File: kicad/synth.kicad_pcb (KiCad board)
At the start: 2 copper layers, 190.5 x 101.6 mm, 265 parts, among them CON101 SD_Card, CON201 K375A (DJK-02A), J301 KATE_3.5MM_6, J302 KATE_3.5MM_6, J401 KATE_3.5MM_6, J402 KATE_3.5MM_6, J403 KATE_3.5MM_6, P101 CONN_01X05, P102 CONN_01X03, P103 CONN_01X03, P104 47346-0001, P105 CONN_01X01, P106 DIN_5, P301 CONN_02X04, Q101 MMBTA42, Q201 FDS6675, Q202 IRF7313PBF, Q301 Si2301DS, SW101 SW_PUSH, SW102 SW_PUSH, T201 TRANS_CUSTOM, U101 STM32F405R, U102 USBLC6-2, U103 AD1955, U104 HCPL0453, U201 LM78L12ACZ, U202 79L12, U203 MC33269-SO8, U204 TPS76333DBV, U205 LP2985LV, U206 LP2985LV, U301 OP275S, U302 OP275S, U303 LM4864, U304 LM4864, U305 OP275S, U401 AD824, Y101 25MHz

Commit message: before moving headphone amp to the left
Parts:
- added P302: CONN_01X03, Pin_Headers:Pin_Header_Straight_1x03, F.Cu at (8.64, 135.5)
- added Q401: Si2301DS, TO_SOT_Packages_SMD:SOT-23, F.Cu at (110.7, 142.5)
- added Q402: Si2301DS, TO_SOT_Packages_SMD:SOT-23, F.Cu at (80.3, 142.0)
- added Q403: Si2301DS, TO_SOT_Packages_SMD:SOT-23, F.Cu at (95.2, 142.2)
- added R421: 10K, Resistors_SMD:R_0805, F.Cu at (110.7, 139.2)
- added R422: 10K, Resistors_SMD:R_0805, F.Cu at (80.0, 135.9)
- added R423: 10K, Resistors_SMD:R_0805, F.Cu at (93.7, 135.9)
- R301, R302, R307, R308: footprint Resistors_SMD:R_0805 -> Resistors_SMD:R_1206
- moved R337 149.0 mm to (12.1, 134.6), turned to 90 degrees
- moved J302 149.0 mm to (5.97, 139.7)
- moved C416 148.3 mm to (155.2, 183.6)
- moved C341 141.8 mm to (9.53, 130.2), turned to 270 degrees
- moved J301 140.6 mm to (42.3, 139.7)
- moved C417 139.6 mm to (129.5, 183.6)
- moved R335 138.8 mm to (12.1, 129.5), turned to 270 degrees
- moved L303 137.3 mm to (49.5, 139.3), turned to 180 degrees
- moved R333 136.5 mm to (12.1, 125.7), turned to 90 degrees
- moved R338 136.0 mm to (0.00, 134.6), turned to 90 degrees
- moved C340 135.6 mm to (6.08, 129.9), turned to 0 degrees
- moved C335 134.3 mm to (14.6, 125.7)
- moved C331 133.7 mm to (48.9, 134.9), turned to 0 degrees
- moved R324 133.1 mm to (14.6, 121.9), turned to 270 degrees
- moved U303 131.9 mm to (48.9, 128.0), turned to 180 degrees
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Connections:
- C318 pad 2: Net-(C318-Pad2) -> GNDA
- C320 pad 2: Net-(C318-Pad2) -> GNDA
- C321 pad 2: Net-(C321-Pad2) -> GNDA
- C322 pad 2: Net-(C322-Pad2) -> GNDA
- C323 pad 2: Net-(C321-Pad2) -> GNDA
- C324 pad 2: Net-(C322-Pad2) -> GNDA
- C336 pad 2: Net-(C336-Pad2) -> GNDA
- C338 pad 2: Net-(C336-Pad2) -> GNDA
- C339 pad 2: Net-(C339-Pad2) -> GNDA
- C340 pad 2: Net-(C339-Pad2) -> GNDA
- J301 pad 1: /audioout/~SHUTDOWN -> /audioout/PHONES_SW
- J301 pad 4: /audioout/~SHUTDOWN -> /audioout/PHONES_SW
- Q301 pad 1: /audioout/~SHUTDOWN -> /audioout/PHONES_SW
- R340 pad 2: /audioout/~SHUTDOWN -> /audioout/PHONES_SW
- R401 pad 2: /audio/LEDPLUG1 -> Net-(Q402-Pad2)
- R402 pad 2: /audio/LEDPLUG2 -> Net-(Q403-Pad2)
- R403 pad 2: /audio/LEDPLUG3 -> Net-(Q401-Pad2)
- U101 pad 40: /audio/LEDPLUG2 -> /LEDPLUG2
- U101 pad 41: /audio/LEDPLUG3 -> /LEDPLUG3
- U101 pad 52: /audio/LEDPLUG1 -> /LEDPLUG1
- U101 pad 62: Net-(U101-Pad62) -> /audioout/PHONES_SW
- U303 pad 1: /audioout/~SHUTDOWN -> /audioout/PHONES_SW
- U304 pad 1: /audioout/~SHUTDOWN -> /audioout/PHONES_SW
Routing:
- net GNDA: track 0.00 -> 366.9 mm, vias 0 -> 22
- net +12VOPA: track 0.00 -> 119.6 mm, vias 0 -> 5
- net -12VOPA: track 0.00 -> 116.2 mm, vias 0 -> 4
- net +3V3A_CPU: track 0.00 -> 112.4 mm
- net /audioout/SE_RIGHT: track 0.00 -> 108.6 mm, vias 0 -> 2
- net /audioout/IOUTR+: track 0.00 -> 97.0 mm
- net /audioout/IOUTR-: track 0.00 -> 80.2 mm
- net /audioout/SE_LEFT: track 0.00 -> 80.2 mm, vias 0 -> 2
- net /audioout/VREF: track 0.00 -> 65.1 mm, vias 0 -> 3
- net GNDD: track 0.00 -> 57.9 mm, vias 0 -> 1
- net /audioout/IOUTL+: track 0.00 -> 56.3 mm
- net (no net): track 0.00 -> 55.5 mm, vias 0 -> 1
- net /audioout/IOUTL-: track 0.00 -> 54.5 mm
- net Net-(C328-Pad1): track 0.00 -> 46.5 mm
- net /audioout/PHONES_SW: track 0.00 -> 42.6 mm
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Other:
- net class Default: via_dia 0.6 -> 1.25
- net class anal added: clearance 0.2, trace_width 0.25, via_dia 1.25, via_drill 0.4
- net class power added: clearance 0.3, trace_width 0.4, via_dia 1.25, via_drill 0.4

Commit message: gruuuu
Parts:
- added Q302: BC817, TO_SOT_Packages_SMD:SOT-23, F.Cu at (92.6, 90.9)
- added R303: 1K, Resistors_SMD:R_0805, F.Cu at (16.3, 144.5)
- added R342: 10K, Resistors_SMD:R_0805, F.Cu at (96.2, 90.7)
- P105: footprint SMD_Packages:1Pin -> Pin_Headers:Pin_Header_Straight_1x01
- R118: footprint Resistors_SMD:R_0402 -> Resistors_SMD:R_0603
- R203: footprint Resistors_SMD:R_0805 -> Resistors_SMD:R_2010
- T201: footprint Transformers_SMPS_ThroughHole:Coilcraft-Q4434-B_Rhombus-T1311 -> trafo_ossi:TRAFO_OSSI
- moved R120 136.2 mm to (32.6, 73.5)
- moved U104 134.6 mm to (27.2, 74.4)
- moved D102 131.9 mm to (20.7, 76.5), turned to 90 degrees
- moved R116 130.7 mm to (21.3, 72.9), turned to 270 degrees
- moved P106 130.4 mm to (29.0, 60.7)
- moved D103 128.2 mm to (42.8, 53.3), turned to 0 degrees
- moved Q101 124.0 mm to (43.9, 57.7)
- moved R121 119.8 mm to (40.8, 57.8), turned to 90 degrees
- moved R122 119.4 mm to (48.4, 55.0), turned to 135 degrees
- moved BT101 101.9 mm to (80.8, -31.8)
- moved P103 95.1 mm to (81.4, 81.7)
- moved CON101 90.3 mm to (136.2, -8.59)
- moved C114 90.0 mm to (127.6, -12.7)
- moved C115 90.0 mm to (127.6, -16.5)
- moved R112 90.0 mm to (110.5, -10.8)
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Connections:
- net /LEDPLUG1 renamed Net-(U101-Pad52)
- net /LEDPLUG2 renamed Net-(U101-Pad40)
- net /LEDPLUG3 renamed Net-(U101-Pad41)
- C201 pad 1: /megapower/+5V_UNREG -> +5VJACK
- C304 pad 1: /audioout/IOUTL- -> /audioout/IOUTL+
- C304 pad 2: /audioout/IOUTL+ -> /audioout/IOUTL-
- D204 pad 2: /megapower/+15V -> +3V3D_CPU
- J301 pad 1: /audioout/PHONES_SW -> /audioout/~SHUTDOWN
- J301 pad 4: /audioout/PHONES_SW -> /audioout/~SHUTDOWN
- Q201 pad 5: /megapower/+5V_UNREG -> +5VJACK
- Q201 pad 6: /megapower/+5V_UNREG -> +5VJACK
- Q201 pad 7: /megapower/+5V_UNREG -> +5VJACK
- Q201 pad 8: /megapower/+5V_UNREG -> +5VJACK
- Q301 pad 1: /audioout/PHONES_SW -> /audioout/~SHUTDOWN
- R305 pad 2: /audioout/IOUTL+ -> /audioout/IOUTL-
- R309 pad 2: /audioout/IOUTL- -> /audioout/IOUTL+
- R311 pad 1: /audioout/IOUTL- -> /audioout/IOUTL+
- R312 pad 1: /audioout/IOUTL+ -> /audioout/IOUTL-
- R315 pad 1: /audioout/IOUTL+ -> /audioout/IOUTL-
- R318 pad 1: /audioout/IOUTL- -> /audioout/IOUTL+
- R319 pad 2: Net-(C325-Pad1) -> Net-(C326-Pad2)
- R320 pad 2: Net-(C326-Pad2) -> Net-(C325-Pad1)
- R340 pad 2: /audioout/PHONES_SW -> /audioout/~SHUTDOWN
- T201 pad 3: Net-(Q202-Pad5) -> Net-(T201-Pad3)
- T201 pad 4: Net-(D202-Pad1) -> Net-(Q202-Pad5)
- T201 pad 5: GNDPWR -> Net-(D202-Pad1)
- T201 pad 6: Net-(D203-Pad2) -> GNDPWR
- T201 pad 7: Net-(D201-Pad2) -> Net-(D203-Pad2)
- T201 pad 8: (no net) -> Net-(D201-Pad2)
- U301 pad 2: /audioout/IOUTL- -> /audioout/IOUTL+
- U301 pad 6: /audioout/IOUTL+ -> /audioout/IOUTL-
- U303 pad 1: /audioout/PHONES_SW -> /audioout/~SHUTDOWN
- U304 pad 1: /audioout/PHONES_SW -> /audioout/~SHUTDOWN
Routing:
- net +3V3D_CPU: track 0.00 -> 277.7 mm, vias 0 -> 4
- net /megapower/+15V: track 0.00 -> 179.9 mm, vias 0 -> 1
- net GNDA: track 366.9 -> 530.8 mm, vias 22 -> 34
- net /megapower/+7V5: track 0.00 -> 155.7 mm, vias 0 -> 3
- net /megapower/-15V: track 0.00 -> 147.2 mm, vias 0 -> 1
- net +3V3A_CPU: track 112.4 -> 246.9 mm, vias 0 -> 2
- net /MIDI_RX: track 0.00 -> 122.8 mm
- net Net-(Q302-Pad1): track 0.00 -> 122.3 mm, vias 0 -> 2
- net GNDD: track 57.9 -> 149.6 mm, vias 1 -> 15
- net /audio/HIGAIN2: track 10.8 -> 97.8 mm, vias 0 -> 2
- net /audio/POT1: track 0.00 -> 84.9 mm, vias 0 -> 2
- net /audio/PLUG_3: track 19.0 -> 103.4 mm, vias 1 -> 4
- net /audioout/LINEOUT_SW: track 4.21 -> 86.8 mm, vias 0 -> 1
- net /audio/POT2: track 0.00 -> 73.3 mm, vias 0 -> 3
- net /audio/PLUG_2: track 19.5 -> 91.5 mm, vias 1 -> 3
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- added copper zone on B.Cu, net GNDA
- added copper zone on F.Cu, net GNDA
- added copper zone on B.Cu, net GNDD
- added copper zone on F.Cu, net GNDD
- added copper zone on B.Cu, net GNDPWR
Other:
- board size 190.5 x 101.6 mm -> 154.9 x 101.6 mm
- net class power: clearance 0.3 -> 0.2

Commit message: drc ok large vias
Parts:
- C114, C115, R112, R113, R114: moved to F.Cu
- C207, C208: moved to B.Cu
- moved C114 137.2 mm to (31.0, 84.7)
- moved CON101 136.9 mm to (40.1, 89.0), turned to 90 degrees
- moved C115 136.6 mm to (31.6, 80.6)
- moved R114 122.8 mm to (34.5, 89.5), turned to 180 degrees
- moved R112 121.9 mm to (34.5, 84.6), turned to 180 degrees
- moved R113 119.4 mm to (34.5, 87.1), turned to 180 degrees
- moved BT101 102.4 mm to (85.7, 70.5), turned to 90 degrees
- moved C112 42.5 mm to (99.7, 67.7), turned to 90 degrees
- moved D204 35.8 mm to (129.8, 101.7), turned to 135 degrees
- moved R205 3.21 mm to (160.8, 109.7), turned to 180 degrees
- moved C207 2.56 mm to (157.5, 86.4), turned to 180 degrees
- moved C208 1.25 mm to (150.9, 86.4), turned to 180 degrees
- moved R204 1.21 mm to (164.0, 109.7)
- moved R102 0.76 mm to (90.9, 75.5)
- moved C105 0.57 mm to (118.1, 82.9)
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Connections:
- C207 pad 1: GNDPWR -> Net-(C207-Pad1)
- C207 pad 2: GNDPWR -> Net-(C207-Pad2)
- C208 pad 1: GNDPWR -> Net-(C208-Pad1)
- C208 pad 2: GNDPWR -> Net-(C208-Pad2)
- C301 pad 2: GNDA -> GNDD
- C302 pad 1: GNDA -> GNDD
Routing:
- net +5VJACK: track 39.8 -> 250.1 mm, vias 1 -> 5
- net /audioout/LF_LEFT: track 0.00 -> 179.7 mm, vias 0 -> 4
- net /audioout/LF_RIGHT: track 0.00 -> 168.8 mm, vias 0 -> 4
- net /SDIO_D0: track 0.00 -> 134.2 mm, vias 0 -> 2
- net +5VA_DAC: track 12.6 -> 122.7 mm, vias 0 -> 2
- net /SDIO_CK: track 0.00 -> 109.0 mm, vias 0 -> 2
- net /SDIO_CMD: track 0.00 -> 98.7 mm, vias 0 -> 2
- net /megapower/VFEEDBACK: track 11.0 -> 81.4 mm, vias 0 -> 4
- net GNDD: track 149.6 -> 217.4 mm, vias 15 -> 25
- net +3V3D_CPU: track 277.7 -> 337.8 mm, vias 4 -> 7
- net +3V3A_CPU: track 246.9 -> 268.9 mm, vias 2 -> 4
- net Net-(BT101-Pad1): track 0.00 -> 20.9 mm, vias 0 -> 1
- net GNDPWR: track 48.6 -> 62.5 mm, vias 5 -> 6
- net GNDA: track 530.8 -> 544.4 mm, vias 34 -> 37
- net /SPI_MOSI: track 61.4 -> 52.2 mm
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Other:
- board size 154.9 x 101.6 mm -> 154.9 x 102.9 mm

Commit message: ok
adding inline resistors on i2s next
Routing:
- net /~DACRST: track 9.86 -> 88.8 mm, vias 0 -> 6
- net /I2S_MCK: track 68.2 -> 73.7 mm
- net GNDD: track 217.4 -> 216.5 mm
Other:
- net class Default: via_dia 1.25 -> 0.9
- net class anal: via_dia 1.25 -> 0.9
- net class power: via_dia 1.25 -> 0.9

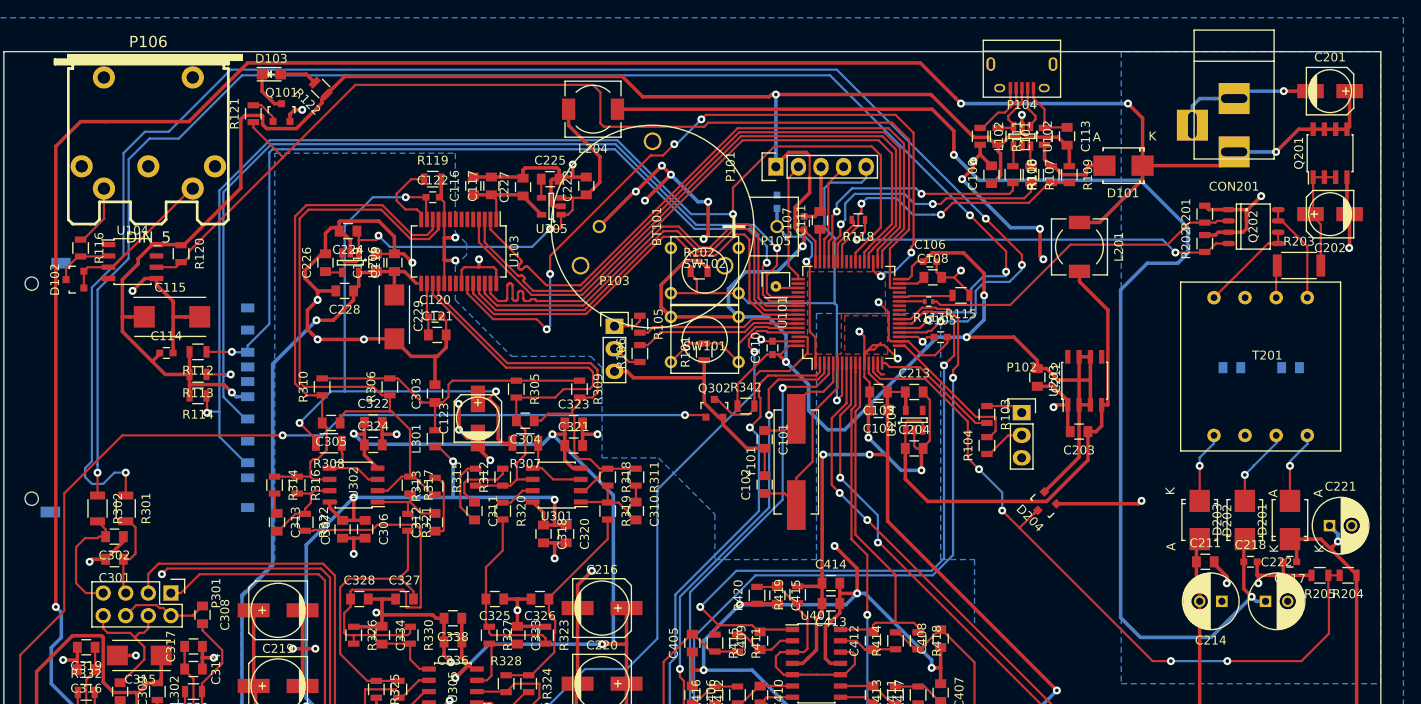
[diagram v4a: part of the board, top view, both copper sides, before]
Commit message: battery is on the wrong side... sigh
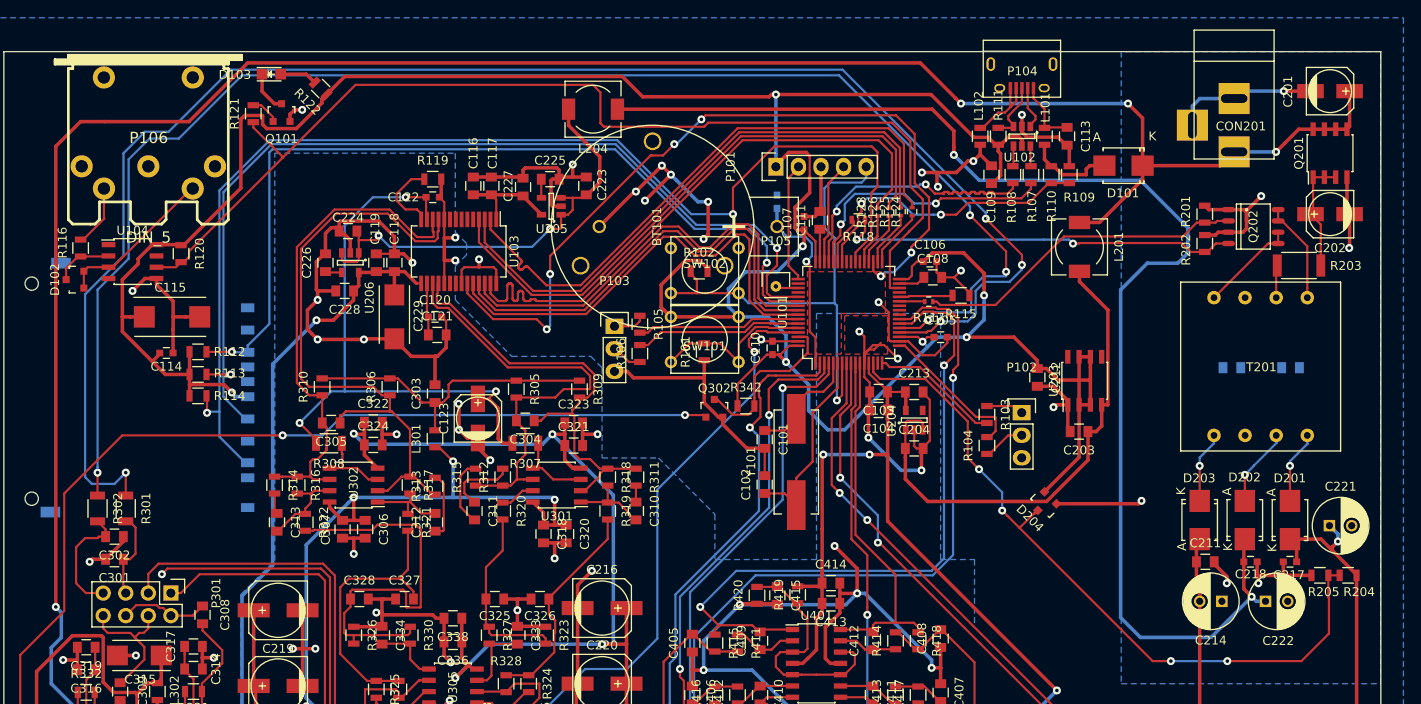
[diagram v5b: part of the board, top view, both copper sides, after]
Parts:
- added R123: 47, Resistors_SMD:R_0402, F.Cu at (111.0, 68.8)
- added R124: 47, Resistors_SMD:R_0402, F.Cu at (114.9, 68.8)
- added R125: 47, Resistors_SMD:R_0402, F.Cu at (113.6, 68.8)
- added R126: 47, Resistors_SMD:R_0402, F.Cu at (112.3, 68.8)
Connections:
- U101 pad 33: /I2S_WS -> /I2S_WS#
- U101 pad 34: /I2S_CK -> /I2S_CK#
- U101 pad 36: /I2S_SD -> /I2S_SD#
- U101 pad 37: /I2S_MCK -> /I2S_MCK#
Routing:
- net GNDD: track 216.5 -> 207.2 mm, vias 25 -> 24
- net /I2S_CK: track 74.0 -> 66.4 mm
- net /I2S_SD: track 73.9 -> 66.9 mm
- net /I2S_WS: track 73.8 -> 67.1 mm
- net /I2S_MCK: track 73.7 -> 67.1 mm
- net /I2S_WS#: track 0.00 -> 6.59 mm
- net /I2S_CK#: track 0.00 -> 6.26 mm
- net /I2S_SD#: track 0.00 -> 6.09 mm
- net /I2S_MCK#: track 0.00 -> 5.76 mm
- net /audioout/IOUTR+: track 74.8 -> 71.3 mm
- net /audioout/IOUTR-: track 58.1 -> 56.0 mm
- net Net-(U101-Pad15): track 1.77 -> 0.00 mm
- net GNDA: track 544.4 -> 542.7 mm
- net /~DACRST: track 88.8 -> 90.2 mm
- net /USB_FS_DP: track 28.7 -> 30.0 mm
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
